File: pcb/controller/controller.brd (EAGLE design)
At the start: 49.8 x 50 mm, 23 parts, among them SW1 EC12E_SW, U1 LCD-16X2NOHOLES

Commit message: Work on controller layout.
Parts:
- removed 3.3V: M01PTH, SparkFun-Connectors:1X01
- removed IO1, IO2: (no value), SparkFun-Connectors:1X03
- removed POWERLED: (no value), led:1206
- removed S1: CM4400, sensor-comus-group:CM4400
- added BLUETOOTH, JP1, JP2: (no value), SparkFun-Connectors:1X04_NO_SILK
- added ETHERNET: M05X2NO_SILK, SparkFun-Connectors:2X5_NOSILK
- added IC1: 74HCT595D, 74xx-eu:SO16
- added JOYSTICK: (no value), SparkFun-Connectors:1X05_NO_SILK
- added L2: WS2812B, adafruit:WS2812B
- added R2: 1k, rcl:M0805
- added R4: 2k, rcl:M0805
- added S2, S3: SWITCH-MOMENTARY-2-SMD-1101NE, SparkFun-Electromechanical:TACTILE-SWITCH-1101NE
- added VIBRATION_SENSOR: M021X02_NO_SILK, SparkFun-Connectors:1X02_NO_SILK
- R3: value 100R -> 470R
- moved POWER 53.8 mm to (2.00, 42.0)
- moved R1 18.9 mm to (21.0, 2.00)
- moved L1 18.4 mm to (20.0, 12.0), turned to 270 degrees
- moved LEDS 16.3 mm to (40.0, 2.00)
- moved R3 15.0 mm to (35.0, 23.0), turned to 180 degrees
- moved SW1 9.00 mm to (9.00, 8.00)
- moved C15 8.00 mm to (2.00, 38.0)
- moved U1 4.00 mm to (34.0, 32.5)
- moved PHOTOCELL 3.54 mm to (34.5, 12.0), turned to 90 degrees
- moved C10 3.00 mm to (42.0, 29.0)
- moved C12 1.00 mm to (39.0, 29.0)
- flipped C1 to the bottom
- flipped C8 to the bottom
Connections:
- new net BLUETOOTH_RX: BLUETOOTH.1, R2.1, R4.2
- new net BLUETOOTH_TX: BLUETOOTH.2, U$1.2
- new net ETHERNET_CLOCK_OUT: ETHERNET.1
- new net ETHERNET_INT: ETHERNET.2
- new net ETHERNET_RESET: ETHERNET.8
- new net ETHERNET_SELECT: ETHERNET.7, U$1.7
- new net ETHERNET_WDL: ETHERNET.3
- new net LCD_SELECT: IC1.12, U$1.5
- new net PIN3: U$1.6
- new net PIN5: U$1.8
- new net PIN6: U$1.9
- new net PIN7: U$1.10
- new net SERIAL_CLOCK: ETHERNET.6, IC1.11, U$1.16
- new net SERIAL_MISO: ETHERNET.4, U$1.15
- new net SERIAL_MOSI: ETHERNET.5, IC1.14, U$1.14
- new net STATUS_LED2: L1.2-DOUT, L2.4-DIN
- net +3V3: now also ETHERNET.9, JP1.3, JP2.3, R3.2; no longer 3.3V.1, POWERLED.A
- net +5V: now also BLUETOOTH.4, IC1.10, IC1.16, JP1.4, JP2.4, L2.1-VDD; no longer IO1.3, IO2.3
- net EXTRA_IO1: now also JP1.2; no longer IO1.2
- net EXTRA_IO2: now also JP2.2; no longer IO2.2
- net GND: now also BLUETOOTH.3, ETHERNET.10, IC1.13, IC1.8, JP1.1, JP2.1, L2.3-GND, R4.1, VIBRATION_SENSOR.1; no longer IO1.1, IO2.1, S1.1
- net LCD_DATA4: now also IC1.3; no longer U$1.7
- net LCD_DATA5: now also IC1.4; no longer U$1.8
- net LCD_DATA6: now also IC1.5; no longer U$1.9
- net LCD_DATA7: now also IC1.6; no longer U$1.10
- net LCD_ENABLE: now also IC1.2; no longer U$1.6
- net LCD_RS: now also IC1.1; no longer U$1.5
- net LEDSTRIP_OUT: now also L2.2-DOUT; no longer L1.2-DOUT
- net N$1: now also R2.2, U$1.1; no longer POWERLED.C, R3.2
- net RADIO_MISO: no longer U$1.15
- net RADIO_MOSI: no longer U$1.14
- net RADIO_SCK: no longer U$1.16
- net SHAKE_SENSOR: now also VIBRATION_SENSOR.2; no longer S1.2
- net V+: now also U$1.24
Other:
- board text added: "TODO: Check size of * Ethernet module * Bluetooth module * Joystick"
- board text removed: "TODO: Check size of * Radio module And make sure they can be mounted at the same time (on top?)."

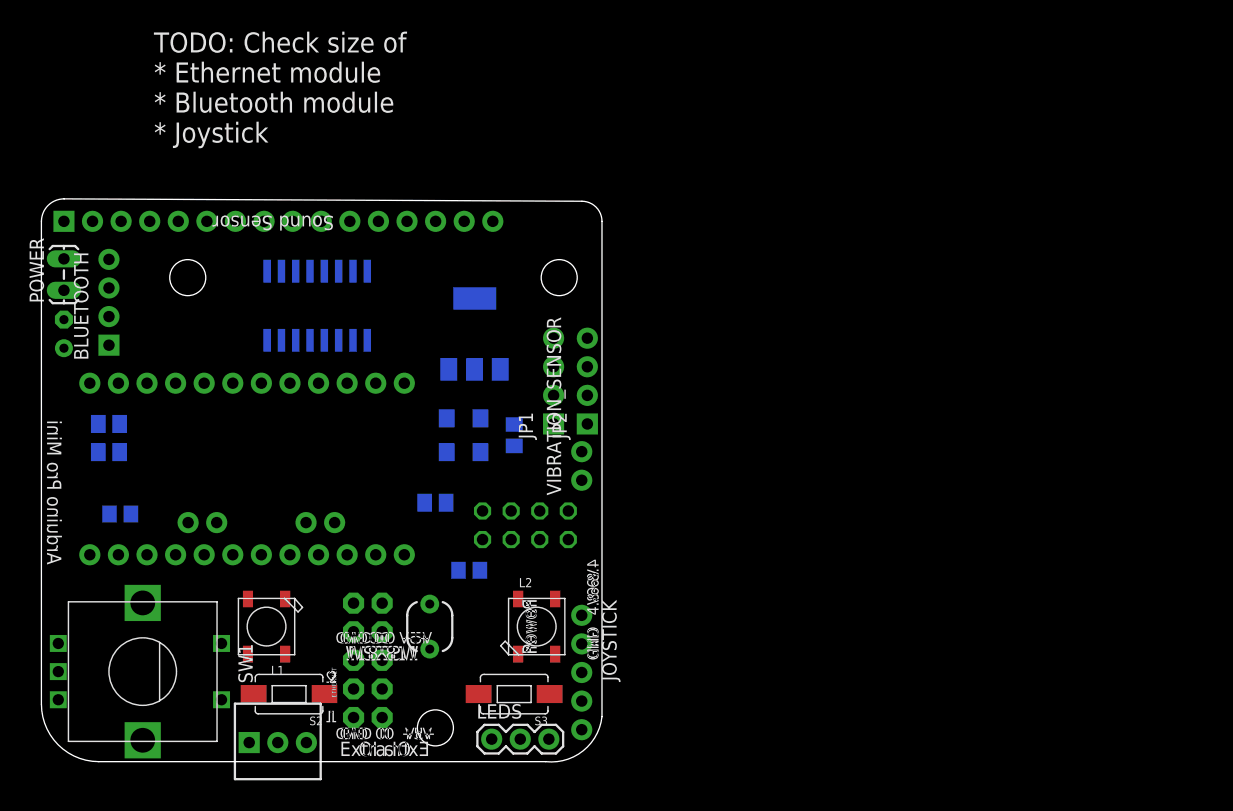
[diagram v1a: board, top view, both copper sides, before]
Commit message: Working on remote controller pcb. Added library with connectors and outlines of some of the used third party modules.
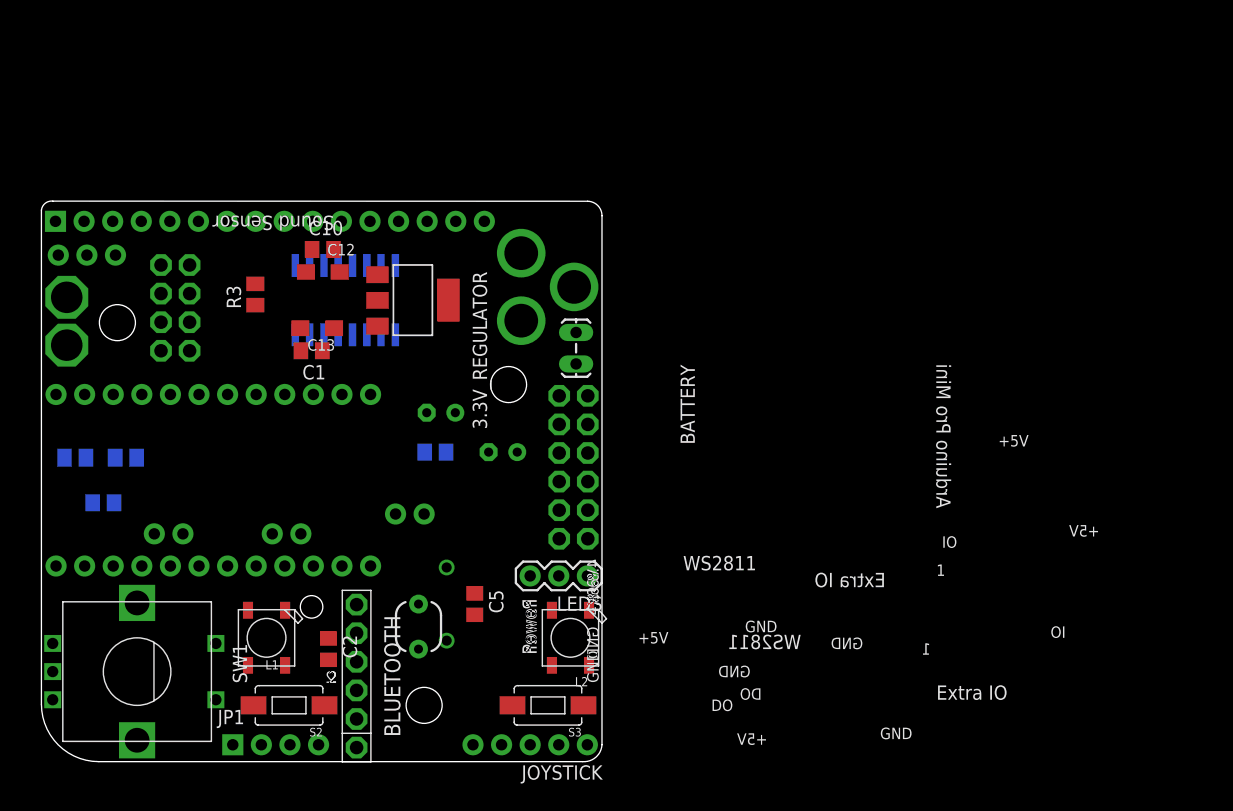
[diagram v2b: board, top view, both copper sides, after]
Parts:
- removed JP2: (no value), SparkFun-Connectors:1X04_NO_SILK
- removed POWER: (no value), SparkFun:1X02_LOCK_LONGPADS
- removed R1: 10k, SparkFun:3362U-2
- added BATTERY: (no value), SparkFun:1X02_LOCK_LONGPADS
- added C2, C4, C5: 100 nF, rcl:C0805
- added C3: 100 uF, rcl:E2,5-6
- added CONTRAST: Trim Pot 10k, SparkFun-Connectors:1X03_NO_SILK
- added EXT_POWER: POWER_JACKPTH, SparkFun-Connectors:POWER_JACK_PTH
- added POWER_SWITCH: KNC1-101-2P, knc1-101-switch:KNC1-101-2P
- added SG1: BUZZERNS, SparkFun-Electromechanical:BUZZER-12MM-NS
- BLUETOOTH: value (none) -> Bluetooth Module; device SparkFun-Connectors:1X04_NO_SILK -> common_modules:BLUETOOTH_MODULE
- ETHERNET: value M05X2NO_SILK -> ENC28J60 Module; device SparkFun-Connectors:2X5_NOSILK -> common_modules:ETHERNET_ENC28J60_MODULE
- RADIO: value NRF24L01 -> NRF28L01 Module; device con-lstb:MA04-2 -> common_modules:NRF24L01_MODULE
- moved LOGO3 43.6 mm to (85.5, 46.0)
- moved BLUETOOTH 42.0 mm to (28.0, 1.25)
- moved C15 40.4 mm to (41.0, 27.5), turned to 0 degrees
- moved JP1 40.3 mm to (17.0, 1.50), turned to 0 degrees
- moved RADIO 35.9 mm to (10.6, 36.5), turned to 90 degrees
- moved ETHERNET 29.0 mm to (46.0, 32.5), turned to 270 degrees
- moved R3 24.5 mm to (19.0, 41.5), flipped to the top, turned to 90 degrees
- moved C1 24.0 mm to (24.0, 36.5), flipped to the top
- moved C10 23.7 mm to (25.0, 45.5), flipped to the top, turned to 0 degrees
- moved C12 20.2 mm to (25.0, 43.5), flipped to the top, turned to 0 degrees
- moved LEDS 16.8 mm to (48.5, 16.5), turned to 180 degrees
- moved C13 14.9 mm to (24.5, 38.5), flipped to the top, turned to 180 degrees
- moved VIBRATION_SENSOR 14.3 mm to (34.0, 22.0), flipped to the bottom, turned to 0 degrees
- moved JOYSTICK 11.5 mm to (48.5, 1.50), turned to 180 degrees
- moved 3.3V_REGULATOR 6.26 mm to (33.0, 41.0), flipped to the top, turned to 270 degrees
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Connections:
- net EXTRA_IO1 renamed EXTRA_IO
- net LCD_SELECT renamed SELECT_LCD
- removed net ETHERNET_RESET: ETHERNET.8
- removed net ETHERNET_SELECT: ETHERNET.7, U$1.7
- removed net ETHERNET_WDL: ETHERNET.3
- removed net EXTRA_IO2: JP2.2, U$1.A5
- removed net PIN3: U$1.6
- removed net PIN5: U$1.8
- removed net PIN6: U$1.9
- removed net PIN7: U$1.10
- removed net RADIO_CE: RADIO.3, U$1.18
- removed net RADIO_CSN: RADIO.4, U$1.17
- removed net RADIO_MISO: RADIO.7
- removed net RADIO_MOSI: RADIO.6
- removed net RADIO_SCK: RADIO.5
- new net BATTERY_GND: BATTERY.1, EXT_POWER.GNDBREAK
- new net BUZZER: C5.1, IC1.15, SG1.+
- new net ETHERNET_WOL: ETHERNET.P$7
- new net JACK_GND: EXT_POWER.GND, POWER_SWITCH.P$2
- new net JOYSTICK_PUSH: JOYSTICK.1, U$1.A5
- new net JOYSTICK_X: JOYSTICK.3, U$1.20
- new net JOYSTICK_Y: JOYSTICK.2, U$1.19
- new net LEFT_BUTTON: S2.P$2, U$1.9
- new net RADIO_ENABLE: RADIO.P$3, U$1.18
- new net RESET: ETHERNET.P$4, U$1.3
- new net RIGHT_BUTTON: S3.P$2, U$1.10
- new net SELECT_ETHERNET: ETHERNET.P$3, U$1.7
- new net SELECT_RADIO: RADIO.P$4, U$1.17
- new net VCC_3.3V: ETHERNET.P$2, RADIO.P$2
- net +3V3: now also C3.+, C4.1; no longer ETHERNET.9, JP2.3, RADIO.2
- net +5V: now also BLUETOOTH.P$5, C2.1, CONTRAST.3, JOYSTICK.4, U1.2; no longer BLUETOOTH.4, JP2.4
- net BLUETOOTH_RX: now also BLUETOOTH.P$2; no longer BLUETOOTH.1
- net BLUETOOTH_TX: now also BLUETOOTH.P$3; no longer BLUETOOTH.2
- net ETHERNET_CLOCK_OUT: now also ETHERNET.P$9; no longer ETHERNET.1
- net ETHERNET_INT: now also ETHERNET.P$10; no longer ETHERNET.2
- net GND: now also BLUETOOTH.P$4, C2.2, C3.-, C4.2, C5.2, CONTRAST.1, ETHERNET.P$1, ETHERNET.P$11, JOYSTICK.5, POWER_SWITCH.P$1, RADIO.P$1, S2.P$1, S3.P$1, SG1.-; no longer BLUETOOTH.3, ETHERNET.10, JP2.1, POWER.1, R1.3, RADIO.1
- net LCD_CONTRAST: now also CONTRAST.2; no longer R1.2
- net RADIO_IRQ: now also RADIO.P$8; no longer RADIO.8
- net ROTARY_PUSH: now also U$1.6; no longer U$1.19
- net SERIAL_CLOCK: now also ETHERNET.P$6, RADIO.P$5; no longer ETHERNET.6
- net SERIAL_MISO: now also ETHERNET.P$8, RADIO.P$7; no longer ETHERNET.4
- net SERIAL_MOSI: now also ETHERNET.P$5, RADIO.P$6; no longer ETHERNET.5
- net STATUS_LED: now also U$1.8; no longer U$1.20
- net V+: now also BATTERY.2, EXT_POWER.PWR; no longer POWER.2, R1.1, U1.2
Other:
- board size 49.8 x 50 mm -> 49.8 x 49.8 mm
- board text removed: "TODO: Check size of * Ethernet module * Bluetooth module * Joystick"

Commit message: Working on routing.
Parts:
- removed C4: 100 nF, rcl:C0805
- added EXTRA_OUT: M02PTH, SparkFun-Connectors:1X02
- C15, C3: value 100 uF -> 10 uF; device rcl:E2,5-6 -> rcl:C0805K
- R3: value 470R -> (470R)
- moved C15 19.9 mm to (23.5, 37.0), flipped to the top, turned to 270 degrees
- moved C3 16.6 mm to (23.5, 42.5), flipped to the top, turned to 90 degrees
- moved C10 5.83 mm to (20.0, 42.5), turned to 90 degrees
- moved C1 4.03 mm to (20.0, 37.0), turned to 270 degrees
- moved C13 2.92 mm to (27.0, 37.0), turned to 270 degrees
- moved R3 2.69 mm to (16.5, 42.5), turned to 270 degrees
- moved C12 2.24 mm to (27.0, 42.5), turned to 90 degrees
- moved R4 2.06 mm to (8.00, 29.0)
- moved R2 2.00 mm to (3.00, 29.0)
- moved VIBRATION_SENSOR 1.50 mm to (35.5, 22.0)
- moved C2 0.79 mm to (24.8, 10.2)
- moved C8 0.71 mm to (6.00, 22.5)
- moved RADIO 0.50 mm to (10.6, 37.0)
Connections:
- removed net +3V3: 3.3V_REGULATOR.2, C10.1, C12.+, C3.+, C4.1, JP1.3, R3.2
- removed net VCC_3.3V: ETHERNET.P$2, RADIO.P$2
- new net +3.3V: 3.3V_REGULATOR.2, C10.1, C12.+, C3.1, ETHERNET.P$2, JP1.3, R3.2, RADIO.P$2
- new net EXTRA_OUTPUT: EXTRA_OUT.1, IC1.7
- net +5V: now also C15.1; no longer C15.+
- net GND: now also C15.2, C3.2, EXTRA_OUT.2; no longer C15.-, C3.-, C4.2
- net LCD_ENABLE: now also IC1.1; no longer IC1.2
- net LCD_RS: now also IC1.2; no longer IC1.1
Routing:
- net GND: track 0.00 -> 261.9 mm, vias 0 -> 5
- net +5V: track 0.00 -> 173.3 mm, vias 0 -> 6
- net SERIAL_CLOCK: track 0.00 -> 81.9 mm
- net SERIAL_MOSI: track 0.00 -> 70.3 mm, vias 0 -> 5
- net V+: track 0.00 -> 64.2 mm, vias 0 -> 1
- net SERIAL_MISO: track 0.00 -> 62.5 mm, vias 0 -> 2
- net RESET: track 0.00 -> 52.5 mm, vias 0 -> 3
- net LCD_BACKLIGHT: track 0.00 -> 44.9 mm, vias 0 -> 4
- net JACK_GND: track 0.00 -> 44.2 mm
- net +3.3V: track 0.00 -> 43.7 mm, vias 0 -> 2
- net BUZZER: track 0.00 -> 38.1 mm, vias 0 -> 3
- net SELECT_ETHERNET: track 0.00 -> 37.8 mm, vias 0 -> 2
- net STATUS_LED2: track 0.00 -> 35.1 mm, vias 0 -> 2
- net SELECT_RADIO: track 0.00 -> 26.1 mm
- net SELECT_LCD: track 0.00 -> 26.0 mm, vias 0 -> 1
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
